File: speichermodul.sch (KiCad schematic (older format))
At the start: 65 parts, among them IC1 6116, P1 CONN_3X2, P2 CONN_01X01, P3 CONN_01X01, P4 CONN_01X01, P5 CONN_01X01, P6 CONN_01X01, P7 CONN_01X01, P8 CONN_02X10, P9 CONN_02X10, SW1 SW_PUSH, SW2 SW_PUSH, U1 7400, U2 74LS08, U3 74LS08, U4 74LS14, U5 74LS540, U6 74LS540

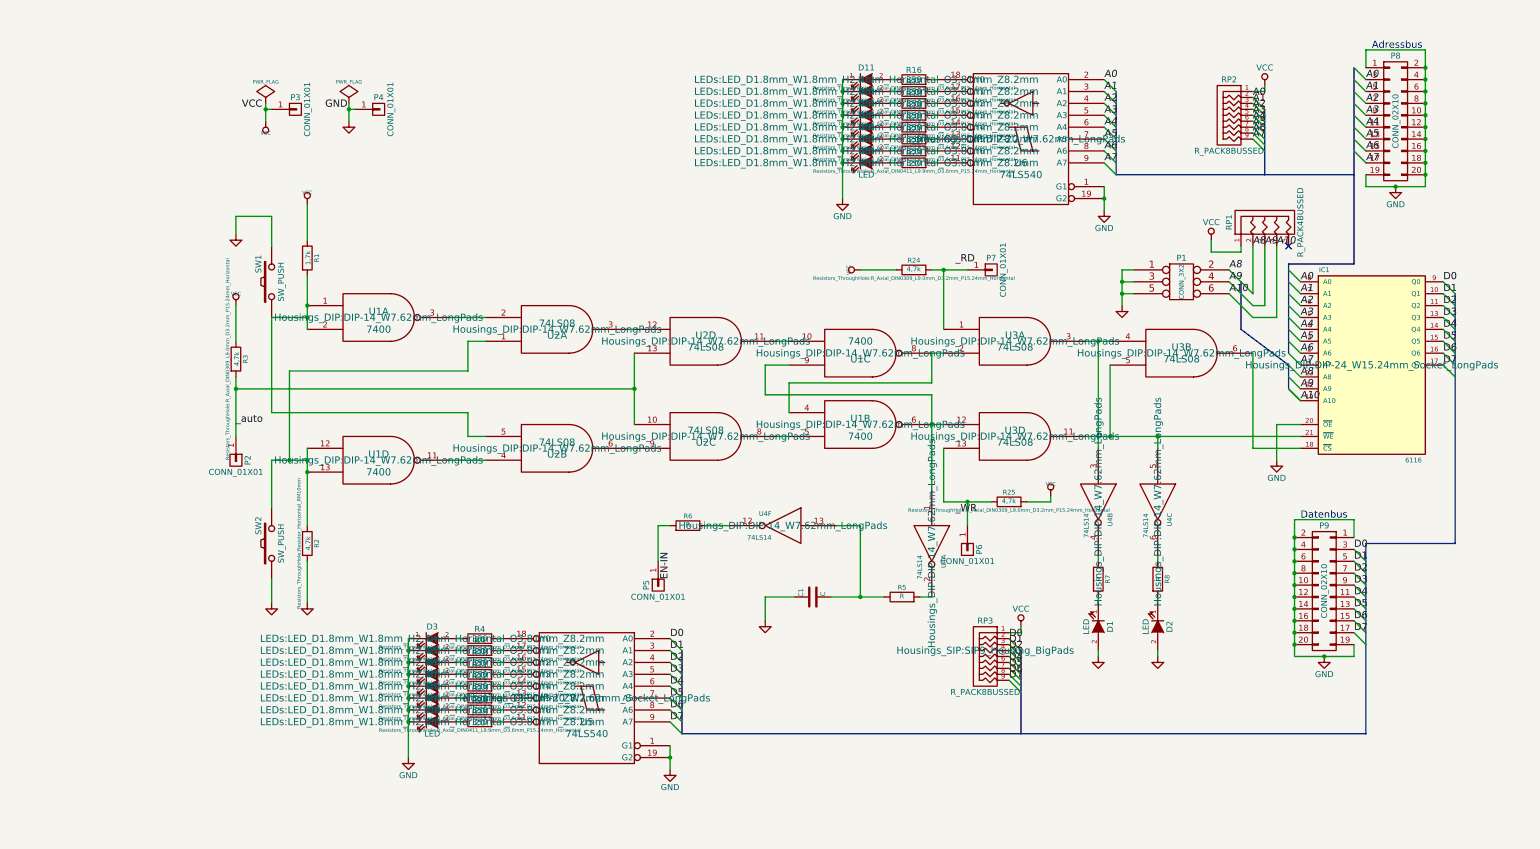
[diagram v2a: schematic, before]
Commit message: einige Footprints geändert
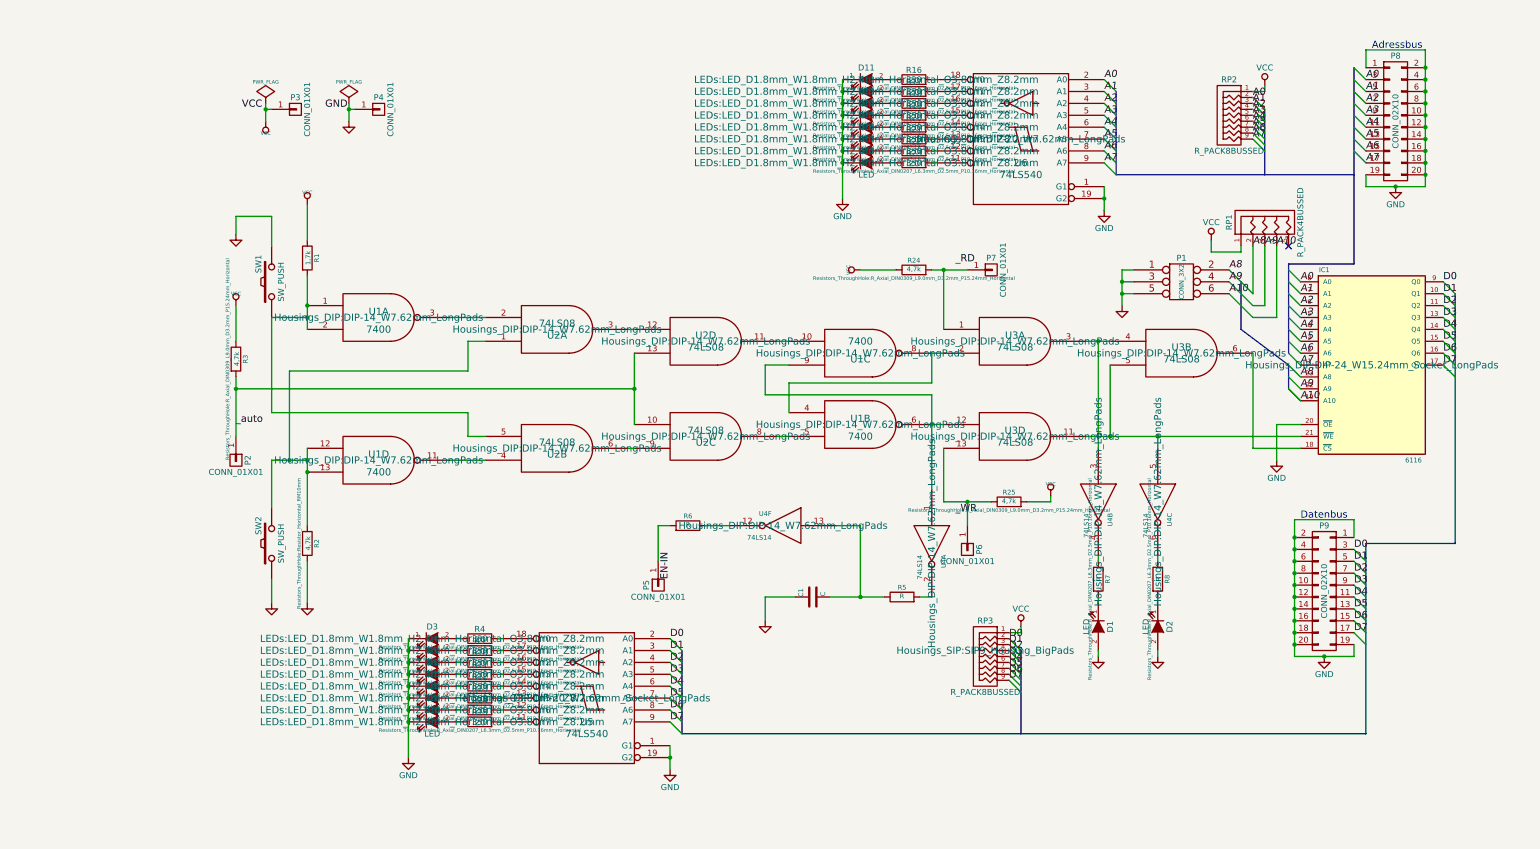
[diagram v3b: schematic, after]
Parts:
- R10, R11, R12, R13, R14, R15, R16, R17, R18, R19, R20, R21, R22, R23, R4, R9: footprint Resistors_ThroughHole:R_Axial_DIN0411_L9.9mm_D3.6mm_P15.24mm_Horizontal -> Resistors_ThroughHole:R_Axial_DIN0207_L6.3mm_D2.5mm_P10.16mm_Horizontal
- R7, R8: footprint (none) -> Resistors_ThroughHole:R_Axial_DIN0207_L6.3mm_D2.5mm_P10.16mm_Horizontal
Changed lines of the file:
@@
 F 0 "R7" V 8030 5150 40  0000 C CNN
 F 1 "R" V 7957 5151 40  0000 C CNN
-F 2 "" V 7880 5150 30  0001 C CNN
+F 2 "Resistors_ThroughHole:R_Axial_DIN0207_L6.3mm_D2.5mm_P10.16mm_Horizontal" V 7880 5150 30  0000 C CNN
 F 3 "~" H 7950 5150 30  0000 C CNN
 	1    7950 5150
@@
 F 0 "R8" V 8530 5150 40  0000 C CNN
 F 1 "R" V 8457 5151 40  0000 C CNN
-F 2 "" V 8380 5150 30  0001 C CNN
+F 2 "Resistors_ThroughHole:R_Axial_DIN0207_L6.3mm_D2.5mm_P10.16mm_Horizontal" V 8380 5150 30  0000 C CNN
 F 3 "~" H 8450 5150 30  0000 C CNN
 	1    8450 5150
@@
 F 0 "R4" V 2830 5650 50  0000 C CNN
 F 1 "330" V 2750 5650 50  0000 C CNN
-F 2 "Resistors_ThroughHole:R_Axial_DIN0411_L9.9mm_D3.6mm_P15.24mm_Horizontal" V 2680 5650 30  0000 C CNN
+F 2 "Resistors_ThroughHole:R_Axial_DIN0207_L6.3mm_D2.5mm_P10.16mm_Horizontal" V 2680 5650 30  0000 C CNN
 F 3 "" H 2750 5650 30  0000 C CNN
 	1    2750 5650
@@
 F 0 "R9" V 2830 5750 50  0000 C CNN
 F 1 "330" V 2750 5750 50  0000 C CNN
-F 2 "Resistors_ThroughHole:R_Axial_DIN0411_L9.9mm_D3.6mm_P15.24mm_Horizontal" V 2680 5750 30  0000 C CNN
+F 2 "Resistors_ThroughHole:R_Axial_DIN0207_L6.3mm_D2.5mm_P10.16mm_Horizontal" V 2680 5750 30  0000 C CNN
 F 3 "" H 2750 5750 30  0000 C CNN
 	1    2750 5750
@@
 F 0 "R10" V 2830 5850 50  0000 C CNN
 F 1 "330" V 2750 5850 50  0000 C CNN
-F 2 "Resistors_ThroughHole:R_Axial_DIN0411_L9.9mm_D3.6mm_P15.24mm_Horizontal" V 2680 5850 30  0000 C CNN
+F 2 "Resistors_ThroughHole:R_Axial_DIN0207_L6.3mm_D2.5mm_P10.16mm_Horizontal" V 2680 5850 30  0000 C CNN
 F 3 "" H 2750 5850 30  0000 C CNN
 	1    2750 5850
@@
 F 0 "R11" V 2830 5950 50  0000 C CNN
 F 1 "330" V 2750 5950 50  0000 C CNN
-F 2 "Resistors_ThroughHole:R_Axial_DIN0411_L9.9mm_D3.6mm_P15.24mm_Horizontal" V 2680 5950 30  0000 C CNN
+F 2 "Resistors_ThroughHole:R_Axial_DIN0207_L6.3mm_D2.5mm_P10.16mm_Horizontal" V 2680 5950 30  0000 C CNN
 F 3 "" H 2750 5950 30  0000 C CNN
 	1    2750 5950
@@
 F 0 "R12" V 2830 6050 50  0000 C CNN
 F 1 "330" V 2750 6050 50  0000 C CNN
-F 2 "Resistors_ThroughHole:R_Axial_DIN0411_L9.9mm_D3.6mm_P15.24mm_Horizontal" V 2680 6050 30  0000 C CNN
+F 2 "Resistors_ThroughHole:R_Axial_DIN0207_L6.3mm_D2.5mm_P10.16mm_Horizontal" V 2680 6050 30  0000 C CNN
 F 3 "" H 2750 6050 30  0000 C CNN
 	1    2750 6050
@@
 F 0 "R13" V 2830 6150 50  0000 C CNN
 F 1 "330" V 2750 6150 50  0000 C CNN
-F 2 "Resistors_ThroughHole:R_Axial_DIN0411_L9.9mm_D3.6mm_P15.24mm_Horizontal" V 2680 6150 30  0000 C CNN
+F 2 "Resistors_ThroughHole:R_Axial_DIN0207_L6.3mm_D2.5mm_P10.16mm_Horizontal" V 2680 6150 30  0000 C CNN
 F 3 "" H 2750 6150 30  0000 C CNN
 	1    2750 6150
@@
 F 0 "R14" V 2830 6250 50  0000 C CNN
 F 1 "330" V 2750 6250 50  0000 C CNN
-F 2 "Resistors_ThroughHole:R_Axial_DIN0411_L9.9mm_D3.6mm_P15.24mm_Horizontal" V 2680 6250 30  0000 C CNN
+F 2 "Resistors_ThroughHole:R_Axial_DIN0207_L6.3mm_D2.5mm_P10.16mm_Horizontal" V 2680 6250 30  0000 C CNN
 F 3 "" H 2750 6250 30  0000 C CNN
 	1    2750 6250
@@
 F 0 "R15" V 2830 6350 50  0000 C CNN
 F 1 "330" V 2750 6350 50  0000 C CNN
-F 2 "Resistors_ThroughHole:R_Axial_DIN0411_L9.9mm_D3.6mm_P15.24mm_Horizontal" V 2680 6350 30  0000 C CNN
+F 2 "Resistors_ThroughHole:R_Axial_DIN0207_L6.3mm_D2.5mm_P10.16mm_Horizontal" V 2680 6350 30  0000 C CNN
 F 3 "" H 2750 6350 30  0000 C CNN
 	1    2750 6350
@@
 F 0 "R16" V 6480 950 50  0000 C CNN
 F 1 "330" V 6400 950 50  0000 C CNN
-F 2 "Resistors_ThroughHole:R_Axial_DIN0411_L9.9mm_D3.6mm_P15.24mm_Horizontal" V 6330 950 30  0000 C CNN
+F 2 "Resistors_ThroughHole:R_Axial_DIN0207_L6.3mm_D2.5mm_P10.16mm_Horizontal" V 6330 950 30  0000 C CNN
 F 3 "" H 6400 950 30  0000 C CNN
 	1    6400 950
@@
 F 0 "R17" V 6480 1050 50  0000 C CNN
 F 1 "330" V 6400 1050 50  0000 C CNN
-F 2 "Resistors_ThroughHole:R_Axial_DIN0411_L9.9mm_D3.6mm_P15.24mm_Horizontal" V 6330 1050 30  0000 C CNN
+F 2 "Resistors_ThroughHole:R_Axial_DIN0207_L6.3mm_D2.5mm_P10.16mm_Horizontal" V 6330 1050 30  0000 C CNN
 F 3 "" H 6400 1050 30  0000 C CNN
 	1    6400 1050
@@
 F 0 "R18" V 6480 1150 50  0000 C CNN
 F 1 "330" V 6400 1150 50  0000 C CNN
-F 2 "Resistors_ThroughHole:R_Axial_DIN0411_L9.9mm_D3.6mm_P15.24mm_Horizontal" V 6330 1150 30  0000 C CNN
+F 2 "Resistors_ThroughHole:R_Axial_DIN0207_L6.3mm_D2.5mm_P10.16mm_Horizontal" V 6330 1150 30  0000 C CNN
 F 3 "" H 6400 1150 30  0000 C CNN
 	1    6400 1150
@@
 F 0 "R19" V 6480 1250 50  0000 C CNN
 F 1 "330" V 6400 1250 50  0000 C CNN
-F 2 "Resistors_ThroughHole:R_Axial_DIN0411_L9.9mm_D3.6mm_P15.24mm_Horizontal" V 6330 1250 30  0000 C CNN
+F 2 "Resistors_ThroughHole:R_Axial_DIN0207_L6.3mm_D2.5mm_P10.16mm_Horizontal" V 6330 1250 30  0000 C CNN
 F 3 "" H 6400 1250 30  0000 C CNN
 	1    6400 1250
@@
 F 0 "R20" V 6480 1350 50  0000 C CNN
 F 1 "330" V 6400 1350 50  0000 C CNN
-F 2 "Resistors_ThroughHole:R_Axial_DIN0411_L9.9mm_D3.6mm_P15.24mm_Horizontal" V 6330 1350 30  0000 C CNN
+F 2 "Resistors_ThroughHole:R_Axial_DIN0207_L6.3mm_D2.5mm_P10.16mm_Horizontal" V 6330 1350 30  0000 C CNN
 F 3 "" H 6400 1350 30  0000 C CNN
 	1    6400 1350
@@
 F 0 "R22" V 6480 1550 50  0000 C CNN
 F 1 "330" V 6400 1550 50  0000 C CNN
-F 2 "Resistors_ThroughHole:R_Axial_DIN0411_L9.9mm_D3.6mm_P15.24mm_Horizontal" V 6330 1550 30  0000 C CNN
+F 2 "Resistors_ThroughHole:R_Axial_DIN0207_L6.3mm_D2.5mm_P10.16mm_Horizontal" V 6330 1550 30  0000 C CNN
 F 3 "" H 6400 1550 30  0000 C CNN
 	1    6400 1550
@@
 F 0 "R23" V 6480 1650 50  0000 C CNN
 F 1 "330" V 6400 1650 50  0000 C CNN
-F 2 "Resistors_ThroughHole:R_Axial_DIN0411_L9.9mm_D3.6mm_P15.24mm_Horizontal" V 6330 1650 30  0000 C CNN
+F 2 "Resistors_ThroughHole:R_Axial_DIN0207_L6.3mm_D2.5mm_P10.16mm_Horizontal" V 6330 1650 30  0000 C CNN
 F 3 "" H 6400 1650 30  0000 C CNN
 	1    6400 1650
@@
 F 0 "R21" V 6480 1450 50  0000 C CNN
 F 1 "330" V 6400 1450 50  0000 C CNN
-F 2 "Resistors_ThroughHole:R_Axial_DIN0411_L9.9mm_D3.6mm_P15.24mm_Horizontal" V 6330 1450 30  0000 C CNN
+F 2 "Resistors_ThroughHole:R_Axial_DIN0207_L6.3mm_D2.5mm_P10.16mm_Horizontal" V 6330 1450 30  0000 C CNN
 F 3 "" H 6400 1450 30  0000 C CNN
 	1    6400 1450

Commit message: Kabel verlegen und pcb layout
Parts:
- P3, P4: footprint (none) -> Pin_Headers:Pin_Header_Straight_1x01_Pitch1.27mm
- SW1, SW2: footprint (none) -> Buttons_Switches_ThroughHole:SW_PUSH_6mm_h5mm
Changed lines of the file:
@@
 F 0 "SW2" H 1150 4960 50  0000 C CNN
 F 1 "SW_PUSH" H 1000 4770 50  0000 C CNN
-F 2 "" H 1000 4850 60  0001 C CNN
+F 2 "Buttons_Switches_ThroughHole:SW_PUSH_6mm_h5mm" H 1000 4850 60  0001 C CNN
 F 3 "~" H 1000 4850 60  0000 C CNN
 	1    1000 4850
@@
 F 0 "SW1" H 1150 2760 50  0000 C CNN
 F 1 "SW_PUSH" H 1000 2570 50  0000 C CNN
-F 2 "" H 1000 2650 60  0001 C CNN
+F 2 "Buttons_Switches_ThroughHole:SW_PUSH_6mm_h5mm" H 1000 2650 60  0001 C CNN
 F 3 "~" H 1000 2650 60  0000 C CNN
 	1    1000 2650
@@
 F 0 "P4" H 1900 1300 50  0000 C CNN
 F 1 "CONN_01X01" V 2000 1200 50  0000 C CNN
-F 2 "" H 1900 1200 60  0001 C CNN
+F 2 "Pin_Headers:Pin_Header_Straight_1x01_Pitch1.27mm" H 1900 1200 60  0001 C CNN
 F 3 "" H 1900 1200 60  0000 C CNN
 	1    1900 1200
@@
 F 0 "P3" H 1200 1300 50  0000 C CNN
 F 1 "CONN_01X01" V 1300 1200 50  0000 C CNN
-F 2 "" H 1200 1200 60  0001 C CNN
+F 2 "Pin_Headers:Pin_Header_Straight_1x01_Pitch1.27mm" H 1200 1200 60  0001 C CNN
 F 3 "" H 1200 1200 60  0000 C CNN
 	1    1200 1200
